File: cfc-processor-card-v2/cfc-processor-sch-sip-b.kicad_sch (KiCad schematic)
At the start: 18 parts, among them U10 RCLAMP0504FB, U7 OSD3358-1G-ISM, Y1 ECS-240-12-30BQ-AEN-TR, Y2 ABS07-32.768KHZ-T

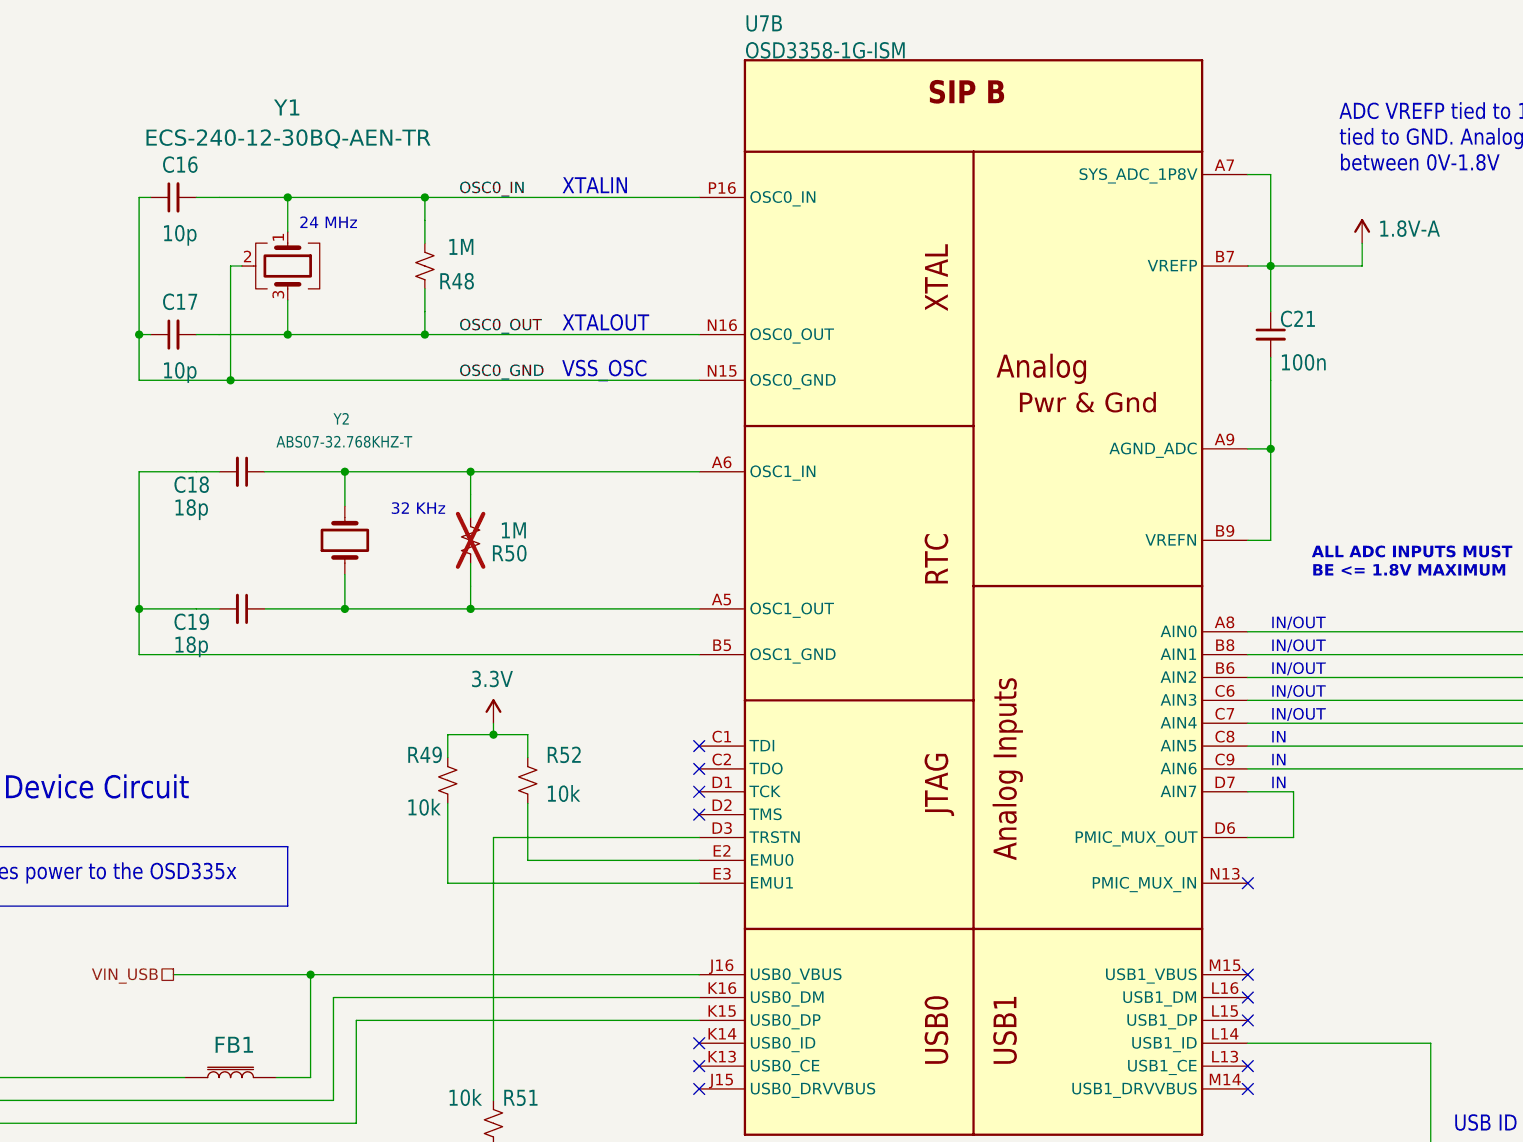
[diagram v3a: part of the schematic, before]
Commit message: Update
Fixed a couple of library issues on testpoints and other misc components. Added Pull up resistors to 8 channel i2c ic
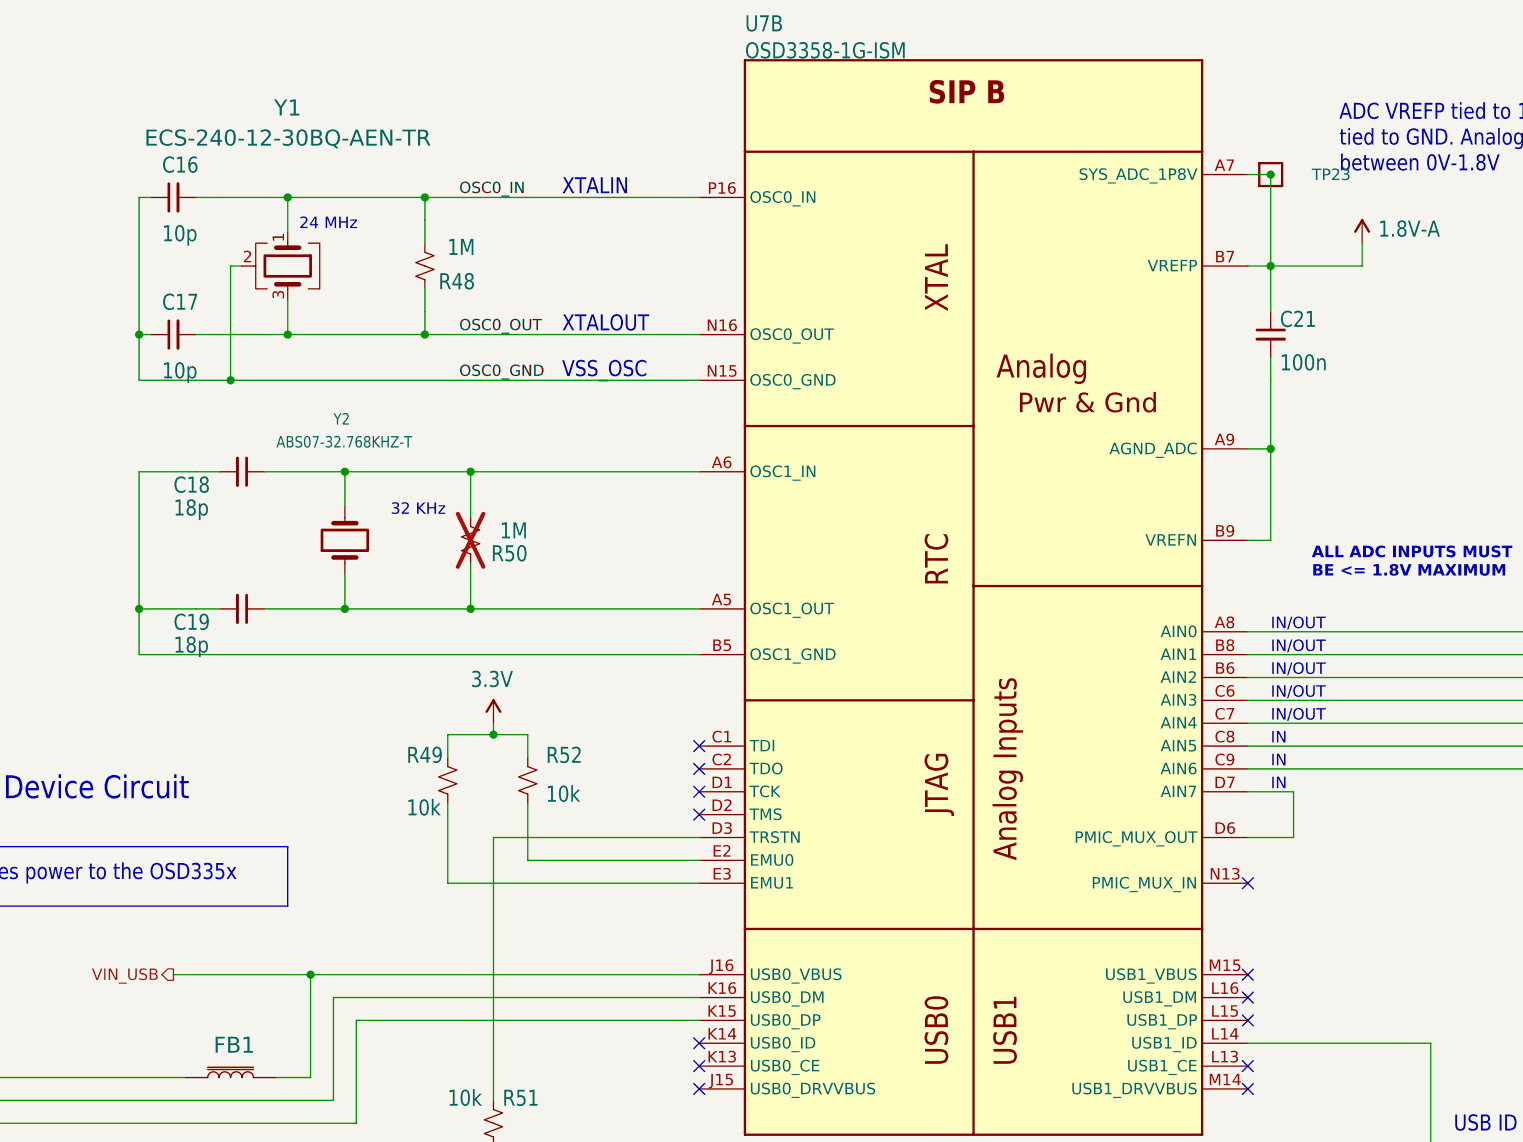
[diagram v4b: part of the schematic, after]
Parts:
- added TP23: TEST-POINT3X4, oresat-misc:TestPoint_Pad_D1.0mm, symbol oresat-misc:Test-Point-1mm-round
- TP83: symbol Oresat Misc:Test-Point-0.75mm-th -> oresat-misc:Test-Point-0.75mm-th
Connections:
- net 1.8V-A: now also TP23.1
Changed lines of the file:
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@@
+	)
+	(junction
+		(at 247.65 69.85)
+		(diameter 0)
+		(color 0 0 0 0)
 	)
 	(junction
@@
 	)
 	(hierarchical_label "VIN_USB"
-		(shape passive)
+		(shape output)
 		(at 125.73 158.75 180)
 		(effects
@@
 				(path "/07ac832f-8d98-4777-b655-1877592dfd88/fb0d8cda-da67-4375-9bc6-6081ff32bfc0"
 					(reference "C19")
+					(unit 1)
+				)
+			)
+		)
+	)
+	(symbol
+		(lib_id "oresat-misc:Test-Point-1mm-round")
+		(at 247.65 69.85 0)
+		(unit 1)
+		(body_style 1)
+		(exclude_from_sim yes)
+		(in_bom no)
+		(on_board yes)
+		(in_pos_files yes)
+		(dnp no)
+		(property "Reference" "TP23"
+			(at 252.222 70.612 0)
+			(show_name no)
+			(do_not_autoplace no)
+			(effects
+				(font
+					(size 1.27 1.27)
+				)
+				(justify left bottom)
+			)
+		)
+		(property "Value" "TEST-POINT3X4"
+			(at 245.11 72.39 0)
+			(hide yes)
+			(show_name no)
+			(do_not_autoplace no)
+			(effects
+				(font
+					(size 1.27 1.27)
+				)
+				(justify left bottom)
+			)
+		)
+		(property "Footprint" "oresat-misc:TestPoint_Pad_D1.0mm"
+			(at 247.65 59.69 0)
+			(hide yes)
+			(show_name no)
+			(do_not_autoplace no)
+			(effects
+				(font
+					(size 1.27 1.27)
+				)
+			)
+		)
+		(property "Datasheet" ""
+			(at 247.65 69.85 0)
+			(hide yes)
+			(show_name no)
+			(do_not_autoplace no)
+			(effects
+				(font
+					(size 1.27 1.27)
+				)
+			)
+		)
+		(property "Description" "1mm round SMT test point"
+			(at 247.65 69.85 0)
+			(hide yes)
+			(show_name no)
+			(do_not_autoplace no)
+			(effects
+				(font
+					(size 1.27 1.27)
+				)
+			)
+		)
+		(pin "1"
+		)
+		(instances
+			(project "cfc-processor"
+				(path "/07ac832f-8d98-4777-b655-1877592dfd88/fb0d8cda-da67-4375-9bc6-6081ff32bfc0"
+					(reference "TP23")
 					(unit 1)
 				)
@@
 	)
 	(symbol
-		(lib_id "Oresat Misc:Test-Point-0.75mm-th")
+		(lib_id "oresat-misc:Test-Point-0.75mm-th")
 		(at 86.36 170.18 180)
 		(unit 1)

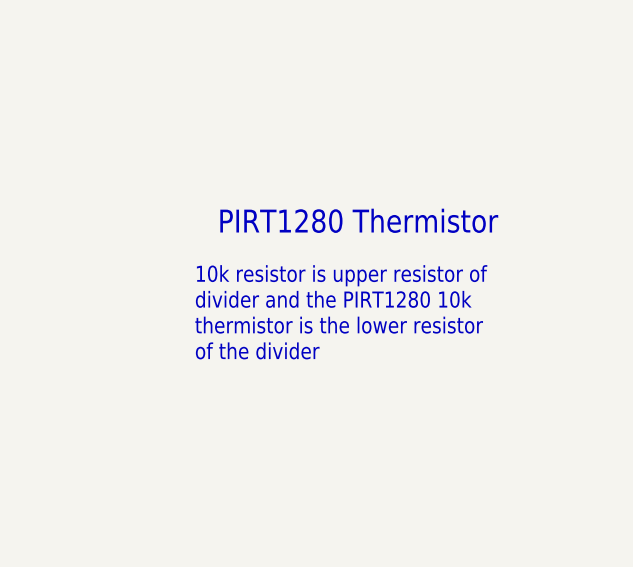
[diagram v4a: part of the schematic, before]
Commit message: Update
Changed passive component footprints to 0603 no silk c. Fixed OPD UART termination resistor on cfc processor card. Added low temp co and tolerance resistor for NTC  thermistor tec voltage divider.
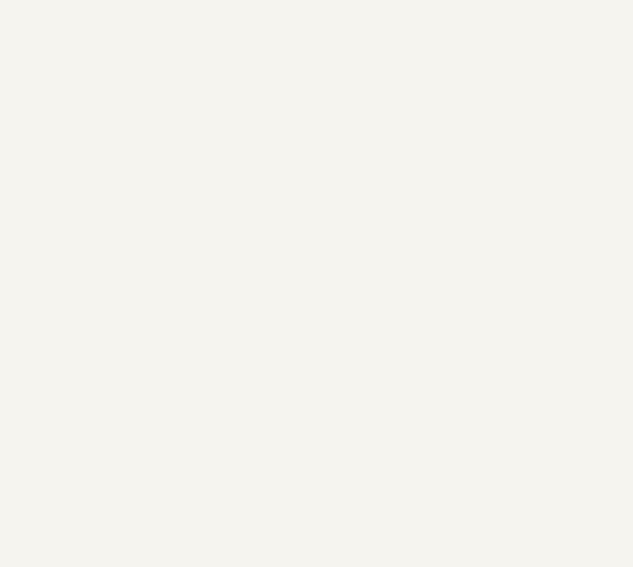
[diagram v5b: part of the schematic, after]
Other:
- note removed: "10k resistor is upper resistor of divider and the PIRT1280 10k thermistor is the lower resistor of the divider"
- note removed: "PIRT1280 Thermistor"
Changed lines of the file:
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@@
-		)
-	)
-	(text "PIRT1280 Thermistor"
-		(exclude_from_sim no)
-		(at 335.28 81.28 0)
-		(effects
-			(font
-				(size 2.54 2.159)
-			)
-			(justify left bottom)
 		)
 	)
@@
 			)
 			(justify left bottom)
-		)
-	)
-	(text "10k resistor is upper resistor of\ndivider and the PIRT1280 10k\nthermistor is the lower resistor\nof the divider"
-		(exclude_from_sim no)
-		(at 332.74 95.25 0)
-		(effects
-			(font
-				(size 1.778 1.5113)
-			)
-			(justify left bottom)

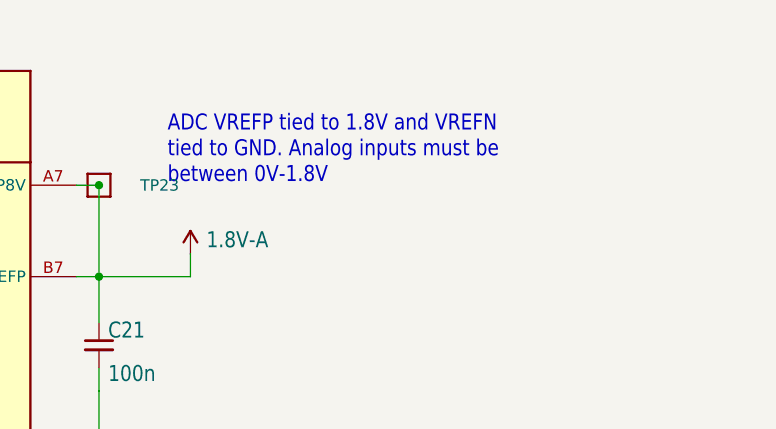
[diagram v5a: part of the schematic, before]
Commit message: update
Changed a couple of test points on OPD to through hole test points. Added tables to DRV8212 on sensor schematic+ other visual improvements to processor schematic.
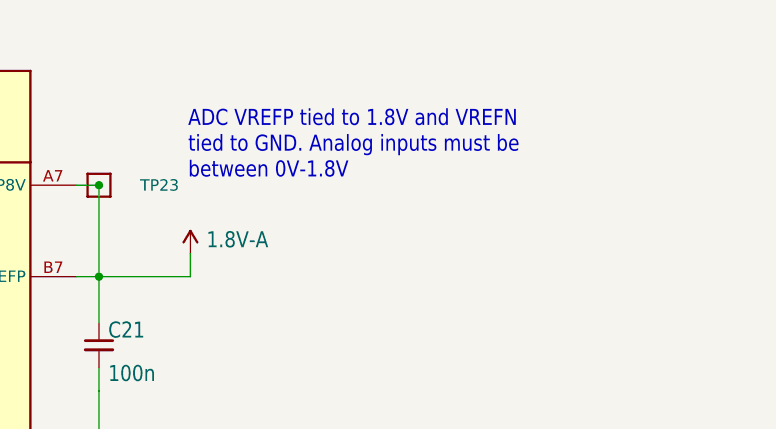
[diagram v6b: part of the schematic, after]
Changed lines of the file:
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@@
 	(text "ADC VREFP tied to 1.8V and VREFN\ntied to GND. Analog inputs must be\nbetween 0V-1.8V"
 		(exclude_from_sim no)
-		(at 255.27 69.85 0)
+		(at 257.556 69.342 0)
 		(effects
 			(font
